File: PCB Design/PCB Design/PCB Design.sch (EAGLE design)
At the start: 5 parts, among them J1 1X2-3.5MM, U1 ADXL337

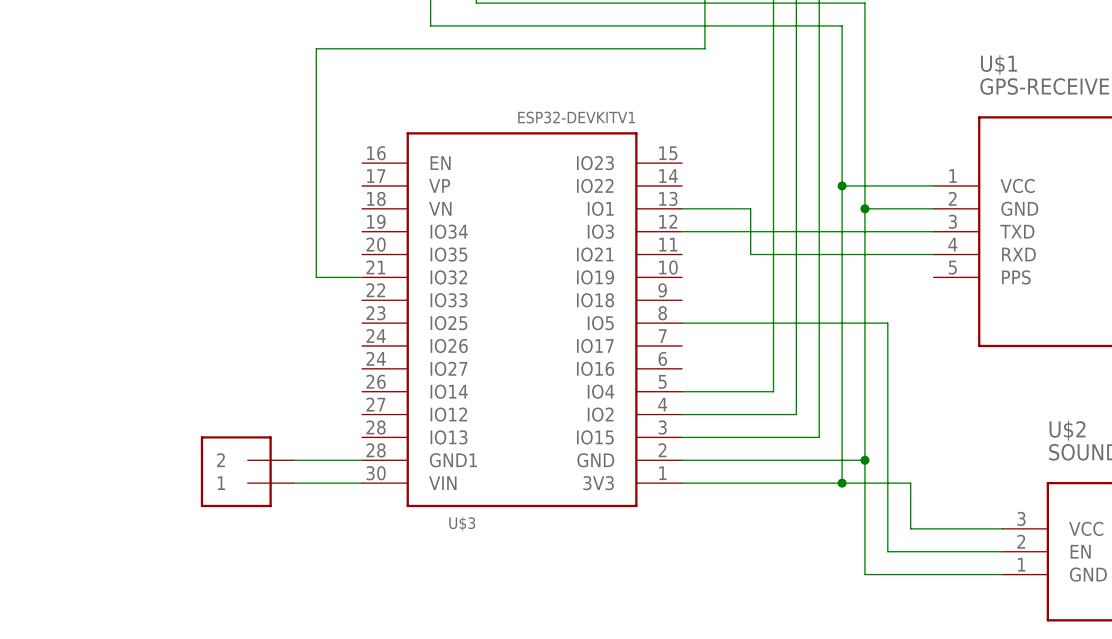
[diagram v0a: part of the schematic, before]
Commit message: Added 5V regulator and board layout
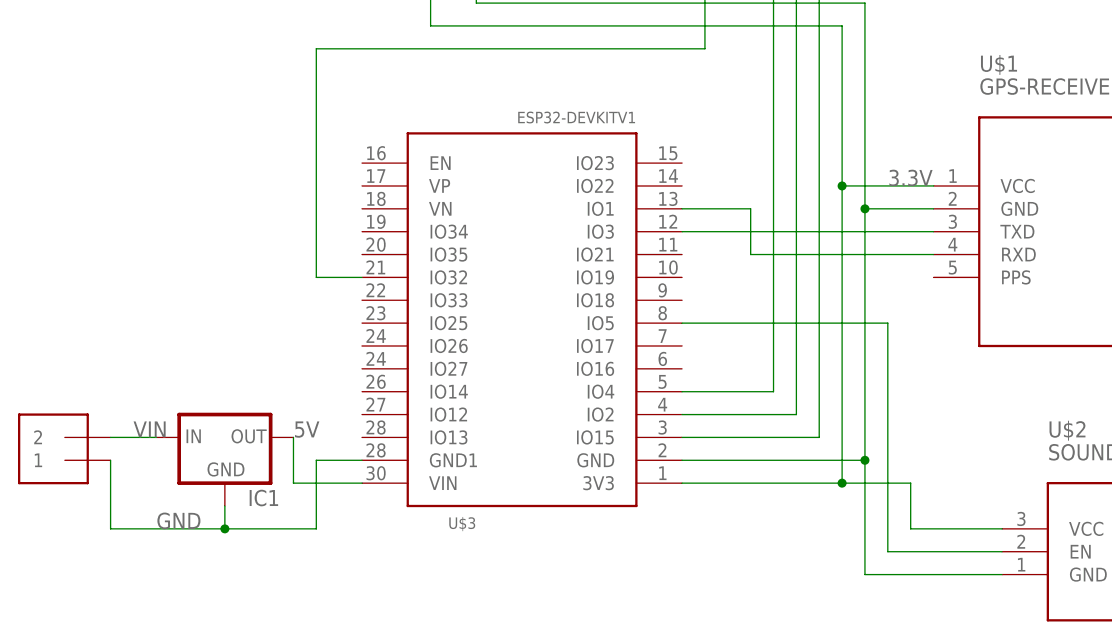
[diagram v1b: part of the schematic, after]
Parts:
- added IC1: (no value), SparkFun:V_REG_78XXSIDE
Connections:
- net N$1 renamed 3.3V
- removed net N$2: U$1.GND, U$2.GND, U$3.GND, U1.GND@1, U1.GND@2
- removed net N$4: J1.1, U$3.VIN
- removed net N$5: J1.2, U$3.GND1
- new net 5V: IC1.OUT, U$3.VIN
- new net GND: IC1.GND, J1.1, U$1.GND, U$2.GND, U$3.GND, U$3.GND1, U1.GND@1, U1.GND@2
- new net VIN: IC1.IN, J1.2
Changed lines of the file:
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@@
 </variantdefs>
 <classes>
-<class number="0" name="default" width="0" drill="0">
+<class number="0" name="default" width="0.2032" drill="0">
+<clearance class="0" value="0.127"/>
+</class>
+<class number="1" name="VIN" width="0.762" drill="0">
+<clearance class="1" value="0.254"/>
+</class>
+<class number="2" name="3.3V" width="0.508" drill="0">
+<clearance class="2" value="0.254"/>
+</class>
+<class number="3" name="5V" width="0.635" drill="0">
+<clearance class="3" value="0.254"/>
 </class>
 </classes>
@@
 <part name="U$3" library="ESP32-DEVKITV1" deviceset="ESP32DEVKITV1" device=""/>
 <part name="J1" library="adafruit" library_urn="urn:adsk.eagle:library:420" deviceset="1X2" device="-3.5MM" package3d_urn="urn:adsk.eagle:package:6240635/1"/>
+<part name="IC1" library="SparkFun" deviceset="V_REG_78XX" device="SIDE"/>
 </parts>
 <sheets>
@@
 <instance part="U1" gate="G$1" x="10.16" y="93.98"/>
 <instance part="U$3" gate="G$1" x="2.54" y="50.8" rot="R90"/>
-<instance part="J1" gate="G$1" x="-27.94" y="30.48" rot="R180"/>
+<instance part="J1" gate="G$1" x="-48.26" y="33.02" rot="R180"/>
+<instance part="IC1" gate="G$1" x="-30.48" y="33.02"/>
 </instances>
 <busses>
 </busses>
 <nets>
-<net name="N$1" class="0">
+<net name="3.3V" class="2">
 <segment>
 <pinref part="U$3" gate="G$1" pin="3V3"/>
@@
 <pinref part="U$2" gate="G$1" pin="VCC"/>
 <wire x1="45.72" y1="22.86" x2="55.88" y2="22.86" width="0.1524" layer="91"/>
+<label x="43.18" y="60.96" size="1.778" layer="95"/>
 </segment>
 </net>
-<net name="N$2" class="0">
+<net name="GND" class="1">
 <segment>
 <wire x1="40.64" y1="81.28" x2="40.64" y2="58.42" width="0.1524" layer="91"/>
@@
 <junction x="-2.54" y="88.9"/>
 </segment>
-</net>
-<net name="N$4" class="0">
-<segment>
-<pinref part="U$3" gate="G$1" pin="VIN"/>
-<pinref part="J1" gate="G$1" pin="1"/>
-<wire x1="-15.24" y1="27.94" x2="-22.86" y2="27.94" width="0.1524" layer="91"/>
-</segment>
-</net>
-<net name="N$5" class="0">
 <segment>
 <pinref part="U$3" gate="G$1" pin="GND1"/>
-<pinref part="J1" gate="G$1" pin="2"/>
-<wire x1="-15.24" y1="30.48" x2="-22.86" y2="30.48" width="0.1524" layer="91"/>
+<wire x1="-15.24" y1="30.48" x2="-20.32" y2="30.48" width="0.1524" layer="91"/>
+<wire x1="-20.32" y1="30.48" x2="-20.32" y2="22.86" width="0.1524" layer="91"/>
+<pinref part="J1" gate="G$1" pin="1"/>
+<wire x1="-20.32" y1="22.86" x2="-30.48" y2="22.86" width="0.1524" layer="91"/>
+<wire x1="-30.48" y1="22.86" x2="-43.18" y2="22.86" width="0.1524" layer="91"/>
+<wire x1="-43.18" y1="22.86" x2="-43.18" y2="30.48" width="0.1524" layer="91"/>
+<pinref part="IC1" gate="G$1" pin="GND"/>
+<wire x1="-30.48" y1="25.4" x2="-30.48" y2="22.86" width="0.1524" layer="91"/>
+<junction x="-30.48" y="22.86"/>
+<label x="-38.1" y="22.86" size="1.778" layer="95"/>
 </segment>
 </net>
@@
 </segment>
 </net>
+<net name="5V" class="3">
+<segment>
+<pinref part="U$3" gate="G$1" pin="VIN"/>
+<pinref part="IC1" gate="G$1" pin="OUT"/>
+<wire x1="-15.24" y1="27.94" x2="-22.86" y2="27.94" width="0.1524" layer="91"/>
+<wire x1="-22.86" y1="27.94" x2="-22.86" y2="33.02" width="0.1524" layer="91"/>
+<label x="-22.86" y="33.02" size="1.778" layer="95"/>
+</segment>
+</net>
+<net name="VIN" class="1">
+<segment>
+<pinref part="IC1" gate="G$1" pin="IN"/>
+<pinref part="J1" gate="G$1" pin="2"/>
+<wire x1="-38.1" y1="33.02" x2="-43.18" y2="33.02" width="0.1524" layer="91"/>
+<label x="-40.64" y="33.02" size="1.778" layer="95"/>
+</segment>
+</net>

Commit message: added team members names and connection points with labels
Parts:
- IC1: MF (none) -> STMICROELECTRONICS; MPN (none) -> L7805ABV; OC_NEWARK (none) -> 34X0689
- J1, U$2, U$3, U1: OC_NEWARK (none) -> unknown
- U$1: MF (none) -> NEOHM - TE CONNECTIVITY; MPN (none) -> YR1B909KCC; OC_NEWARK (none) -> 98K3962
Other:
- note added: "Team 14 Hayden Pietsch Amanda Vuong Jaxon Coward Erick I. Cortez Valdez"
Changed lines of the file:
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@@
 </classes>
 <parts>
-<part name="U$1" library="diy-modules" deviceset="GPS-RECEIVER-NEO6M" device=""/>
-<part name="U$2" library="diy-modules" deviceset="SOUND-BUZZER" device=""/>
-<part name="U1" library="SparkFun-Sensors" deviceset="ADXL337" device=""/>
-<part name="U$3" library="ESP32-DEVKITV1" deviceset="ESP32DEVKITV1" device=""/>
-<part name="J1" library="adafruit" library_urn="urn:adsk.eagle:library:420" deviceset="1X2" device="-3.5MM" package3d_urn="urn:adsk.eagle:package:6240635/1"/>
-<part name="IC1" library="SparkFun" deviceset="V_REG_78XX" device="SIDE"/>
+<part name="U$1" library="diy-modules" deviceset="GPS-RECEIVER-NEO6M" device="">
+<attribute name="MF" value="NEOHM - TE CONNECTIVITY"/>
+<attribute name="MPN" value="YR1B909KCC"/>
+<attribute name="OC_NEWARK" value="98K3962"/>
+</part>
+<part name="U$2" library="diy-modules" deviceset="SOUND-BUZZER" device="">
+<attribute name="MF" value=""/>
+<attribute name="MPN" value=""/>
+<attribute name="OC_NEWARK" value="unknown"/>
+</part>
+<part name="U1" library="SparkFun-Sensors" deviceset="ADXL337" device="">
+<attribute name="MF" value=""/>
+<attribute name="MPN" value=""/>
+<attribute name="OC_NEWARK" value="unknown"/>
+</part>
+<part name="U$3" library="ESP32-DEVKITV1" deviceset="ESP32DEVKITV1" device="">
+<attribute name="MF" value=""/>
+<attribute name="MPN" value=""/>
+<attribute name="OC_NEWARK" value="unknown"/>
+</part>
+<part name="J1" library="adafruit" library_urn="urn:adsk.eagle:library:420" deviceset="1X2" device="-3.5MM" package3d_urn="urn:adsk.eagle:package:6240635/1">
+<attribute name="MF" value=""/>
+<attribute name="MPN" value=""/>
+<attribute name="OC_NEWARK" value="unknown"/>
+</part>
+<part name="IC1" library="SparkFun" deviceset="V_REG_78XX" device="SIDE">
+<attribute name="MF" value="STMICROELECTRONICS"/>
+<attribute name="MPN" value="L7805ABV"/>
+<attribute name="OC_NEWARK" value="34X0689"/>
+</part>
 </parts>
 <sheets>
@@
 <plain>
 <text x="-10.16" y="104.14" size="1.778" layer="91">ST should be 0 unless testing functionality</text>
+<text x="-48.26" y="53.34" size="1.778" layer="91">Team 14
+Hayden Pietsch
+Amanda Vuong
+Jaxon Coward
+Erick I. Cortez Valdez</text>
 </plain>
 <instances>
-<instance part="U$1" gate="G$1" x="68.58" y="55.88"/>
-<instance part="U$2" gate="G$1" x="73.66" y="20.32"/>
-<instance part="U1" gate="G$1" x="10.16" y="93.98"/>
-<instance part="U$3" gate="G$1" x="2.54" y="50.8" rot="R90"/>
-<instance part="J1" gate="G$1" x="-48.26" y="33.02" rot="R180"/>
-<instance part="IC1" gate="G$1" x="-30.48" y="33.02"/>
+<instance part="U$1" gate="G$1" x="68.58" y="55.88">
+<attribute name="OC_NEWARK" x="68.58" y="55.88" size="1.778" layer="96" display="off"/>
+<attribute name="MF" x="68.58" y="55.88" size="1.778" layer="96" display="off"/>
+<attribute name="MPN" x="68.58" y="55.88" size="1.778" layer="96" display="off"/>
+</instance>
+<instance part="U$2" gate="G$1" x="73.66" y="20.32">
+<attribute name="OC_NEWARK" x="73.66" y="20.32" size="1.778" layer="96" display="off"/>
+<attribute name="MF" x="73.66" y="20.32" size="1.778" layer="96" display="off"/>
+<attribute name="MPN" x="73.66" y="20.32" size="1.778" layer="96" display="off"/>
+</instance>
+<instance part="U1" gate="G$1" x="10.16" y="93.98">
+<attribute name="OC_NEWARK" x="10.16" y="93.98" size="1.778" layer="96" display="off"/>
+<attribute name="MF" x="10.16" y="93.98" size="1.778" layer="96" display="off"/>
+<attribute name="MPN" x="10.16" y="93.98" size="1.778" layer="96" display="off"/>
+</instance>
+<instance part="U$3" gate="G$1" x="2.54" y="50.8" rot="R90">
+<attribute name="OC_NEWARK" x="2.54" y="50.8" size="1.778" layer="96" display="off"/>
+<attribute name="MF" x="2.54" y="50.8" size="1.778" layer="96" display="off"/>
+<attribute name="MPN" x="2.54" y="50.8" size="1.778" layer="96" display="off"/>
+</instance>
+<instance part="J1" gate="G$1" x="-48.26" y="33.02" rot="R180">
+<attribute name="OC_NEWARK" x="-48.26" y="33.02" size="1.778" layer="96" display="off"/>
+<attribute name="MF" x="-48.26" y="33.02" size="1.778" layer="96" display="off"/>
+<attribute name="MPN" x="-48.26" y="33.02" size="1.778" layer="96" display="off"/>
+</instance>
+<instance part="IC1" gate="G$1" x="-30.48" y="33.02">
+<attribute name="OC_NEWARK" x="-30.48" y="33.02" size="1.778" layer="96" display="off"/>
+<attribute name="MF" x="-30.48" y="33.02" size="1.778" layer="96" display="off"/>
+<attribute name="MPN" x="-30.48" y="33.02" size="1.778" layer="96" display="off"/>
+</instance>
 </instances>
 <busses>
@@
 </drawing>
 <compatibility>
+<note version="6.3" minversion="6.2.2" severity="warning">
+Since Version 6.2.2 text objects can contain more than one line,
+which will not be processed correctly with this version.
+</note>
 <note version="8.2" severity="warning">
 Since Version 8.2, EAGLE supports online libraries. The ids
